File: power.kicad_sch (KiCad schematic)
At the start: 89 parts, among them J2 Molex_Mini-Fit_2x3_50362462, Q16 DMG1012T-7, Q23 SISS05DN-T1-GE3, Q24 SISS05DN-T1-GE3, Q25 SISS05DN-T1-GE3, Q31 BSS84PH6327XTSA2, Q32 SISS05DN-T1-GE3, Q33 SISS05DN-T1-GE3, Q39 2N7002_SOT-23-3, Q4 DMG1012T-7, Q41 SISS05DN-T1-GE3, Q42 SISS05DN-T1-GE3, Q5 SISS05DN-T1-GE3, Q6 DMG1012T-7, Q9 SISS05DN-T1-GE3, U15 NCP718BSN330T1G, U61 LTC4412IS6, U62 LTC4412IS6, U63 LTC4412IS6, U64 LTC4412IS6, U9 MAX16013

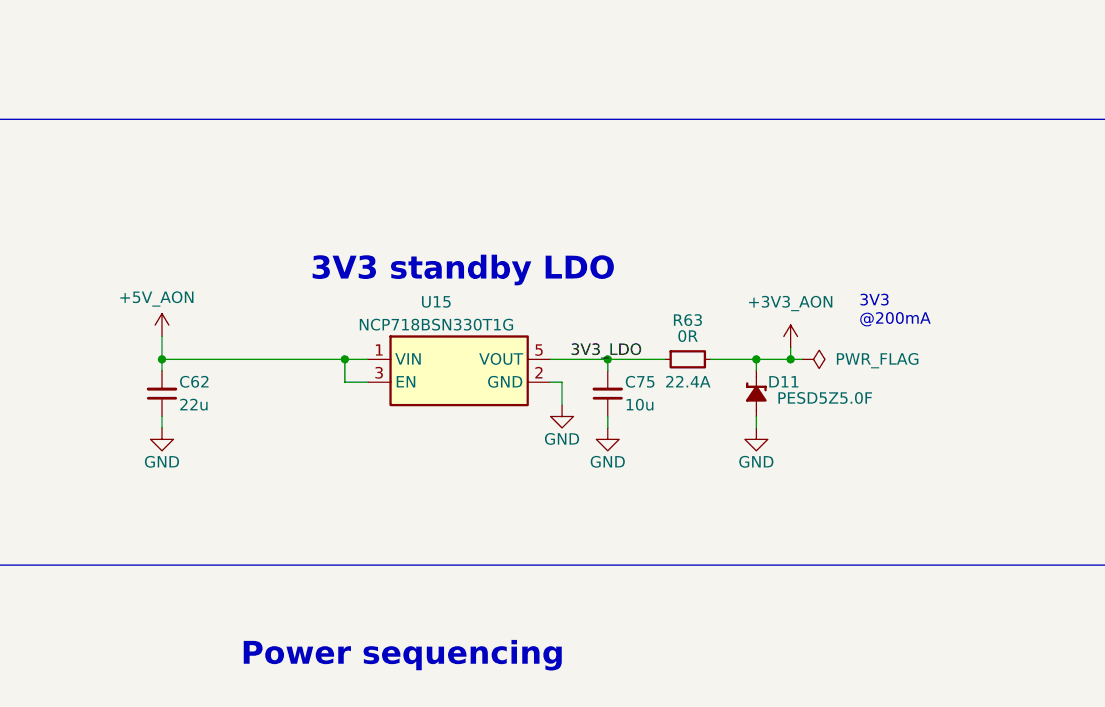
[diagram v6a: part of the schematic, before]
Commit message: [#89645] Replace SYS_VIN_SV LDO with LD39100PUR
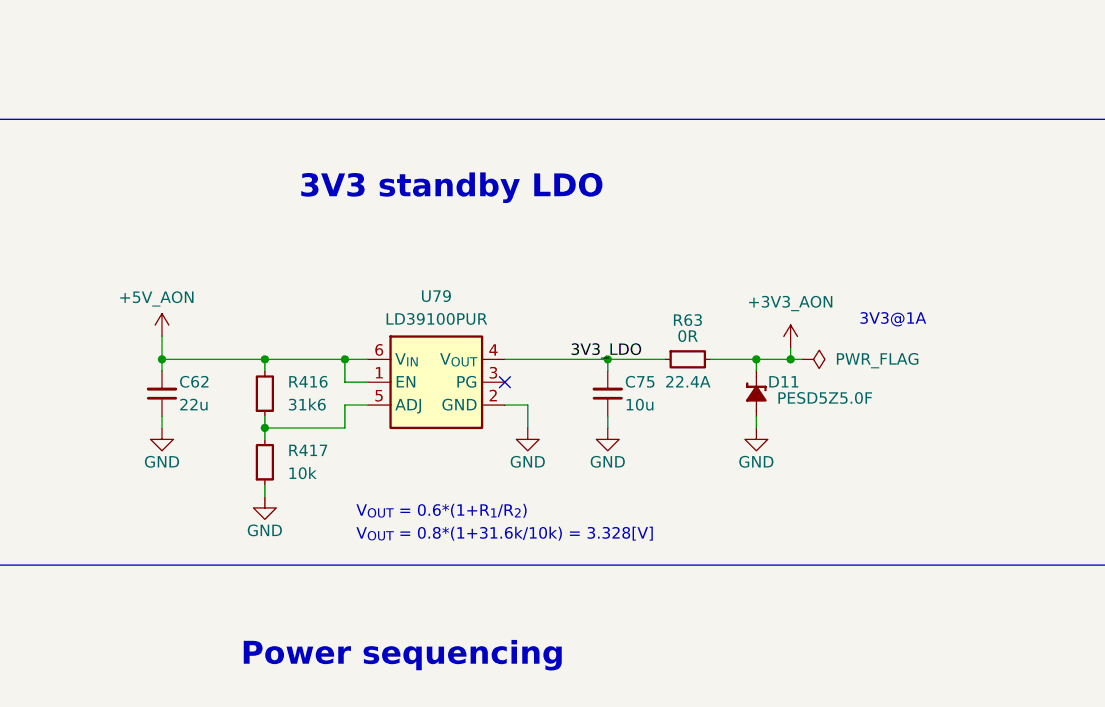
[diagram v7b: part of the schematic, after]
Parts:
- removed U15: NCP718BSN330T1G, antmicro-footprints:SOT-23-5, symbol antmicroPMICVoltageRegulatorsLinear:NCP718BSN330T1G
- added R416: R_31k6_0402, antmicro-footprints:R_0402_1005Metric, symbol antmicroResistors0402:R_31k6_0402
- added R417: R_10k_0402, antmicro-footprints:R_0402_1005Metric, symbol antmicroResistors0402:R_10k_0402
- added U79: LD39100PUR, antmicro-footprints:DFN-6-1EP_3x3mm_P1mm_EP1.5x2.4mm, symbol antmicroPMICVoltageRegulatorsLinear:LD39100PUR
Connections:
- net +5V_AON: now also R416.2, U79.1 (EN), U79.6 (V_{IN})
- net 3V3_LDO: now also U79.4 (V_{OUT})
- net GND: now also R417.1, U79.2 (GND), U79.7 (GND)
- new net: R416.1, R417.2, U79.5 (ADJ)
- no-connect marks 4 -> 5
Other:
- note added: "3V3@1A"
- note added: "V_{OUT} = 0.6*(1+R_{1}/R_{2})"
- note added: "V_{OUT} = 0.8*(1+31.6k/10k) = 3.328[V]"
- note removed: "3V3 @200mA"

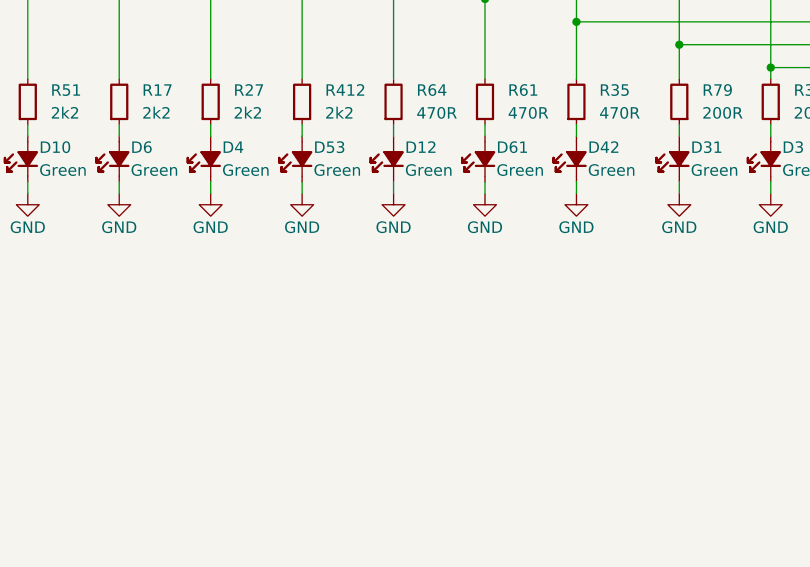
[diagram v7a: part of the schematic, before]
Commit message: [#89645] Add lightpipe for boot and power LED under the power connector
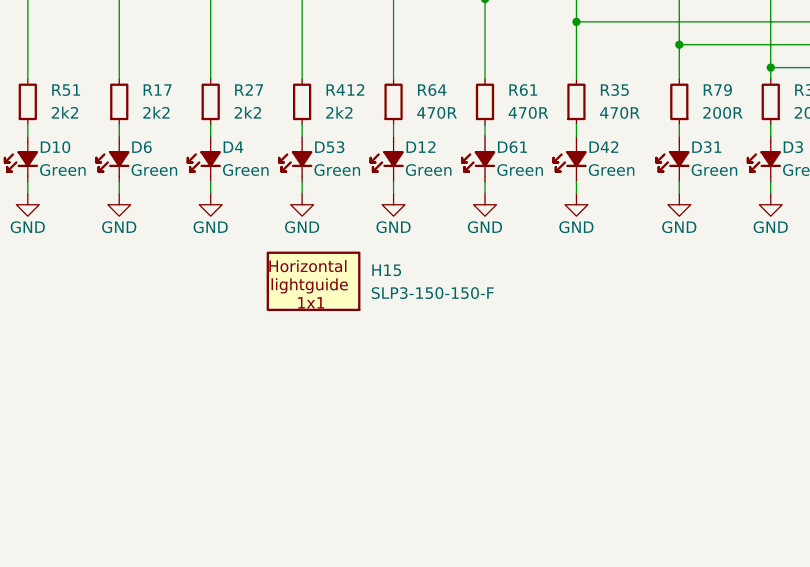
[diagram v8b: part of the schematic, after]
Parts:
- added H15: Lightpipe_Bivar_SLP3-150-150-F, antmicro-footprints:Mech_Lightpipe_Bivar_SLP3-150-150-F, symbol antmicroMechanicalParts:Lightpipe_Bivar_SLP3-150-150-F
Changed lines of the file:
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@@
+	)
+	(symbol
+		(lib_id "antmicroMechanicalParts:Lightpipe_Bivar_SLP3-150-150-F")
+		(at 250.19 227.33 0)
+		(unit 1)
+		(exclude_from_sim no)
+		(in_bom yes)
+		(on_board yes)
+		(dnp no)
+		(fields_autoplaced yes)
+		(property "Reference" "H15"
+			(at 256.54 225.7617 0)
+			(effects
+				(font
+					(size 1.27 1.27)
+					(thickness 0.15)
+				)
+				(justify left)
+			)
+		)
+		(property "Value" "Lightpipe_Bivar_SLP3-150-150-F"
+			(at 261.95 234.645 0)
+			(effects
+				(font
+					(size 1.27 1.27)
+					(thickness 0.15)
+				)
+				(justify left bottom)
+				(hide yes)
+			)
+		)
+		(property "Footprint" "antmicro-footprints:Mech_Lightpipe_Bivar_SLP3-150-150-F"
+			(at 261.95 237.185 0)
+			(effects
+				(font
+					(size 1.27 1.27)
+					(thickness 0.15)
+				)
+				(justify left bottom)
+				(hide yes)
+			)
+		)
+		(property "Datasheet" "https://eu.mouser.com/datasheet/2/50/Bivar_SLP3_150_XXX_X_N-3318840.pdf"
+			(at 261.95 239.725 0)
+			(effects
+				(font
+					(size 1.27 1.27)
+					(thickness 0.15)
+				)
+				(justify left bottom)
+				(hide yes)
+			)
+		)
+		(property "Description" "LED Light Pipe, Rigid Board, Horizontal"
+			(at 261.95 249.885 0)
+			(effects
+				(font
+					(size 1.27 1.27)
+				)
+				(justify left bottom)
+				(hide yes)
+			)
+		)
+		(property "Manufacturer" "BIVAR"
+			(at 261.95 242.265 0)
+			(effects
+				(font
+					(size 1.27 1.27)
+					(thickness 0.15)
+				)
+				(justify left bottom)
+				(hide yes)
+			)
+		)
+		(property "MPN" "SLP3-150-150-F"
+			(at 256.54 228.3017 0)
+			(effects
+				(font
+					(size 1.27 1.27)
+					(thickness 0.15)
+				)
+				(justify left)
+			)
+		)
+		(property "Author" "Antmicro"
+			(at 261.95 244.805 0)
+			(effects
+				(font
+					(size 1.27 1.27)
+					(thickness 0.15)
+				)
+				(justify left bottom)
+				(hide yes)
+			)
+		)
+		(property "License" "Apache-2.0"
+			(at 261.95 247.345 0)
+			(effects
+				(font
+					(size 1.27 1.27)
+					(thickness 0.15)
+				)
+				(justify left bottom)
+				(hide yes)
+			)
+		)
+		(instances
+			(project "jetson-agx-thor-baseboard"
+				(path "/f569b0be-0afd-48b7-93ee-28582a4c645c/18ddd5dc-52e2-402c-b2e2-8bb33f110eab"
+					(reference "H15")
+					(unit 1)
+				)
+			)
+		)
 	)
 	(symbol
